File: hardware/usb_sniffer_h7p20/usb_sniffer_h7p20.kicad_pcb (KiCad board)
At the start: 4 copper layers, 45 x 45 mm, 149 parts, among them J2 USB_C_Receptacle_USB2.0_16P, J3 USB_A, J4 USB_C_Receptacle_USB2.0_16P, J5 FFC-40P-0.5mm,NC, U1 H7P20N0L128-M3H1, U11 EA3036C, U2 LM2903, U3 LM2903, U4 LM2903, U5 USB3343, U6 P25Q32SH-SSH-IT, U7 CY7C68013A-56LTX, U8 24C64BN, U9 CJ3439KDW, X1 XO32,26M,NC, Y1 26M,NC, Y2 24M

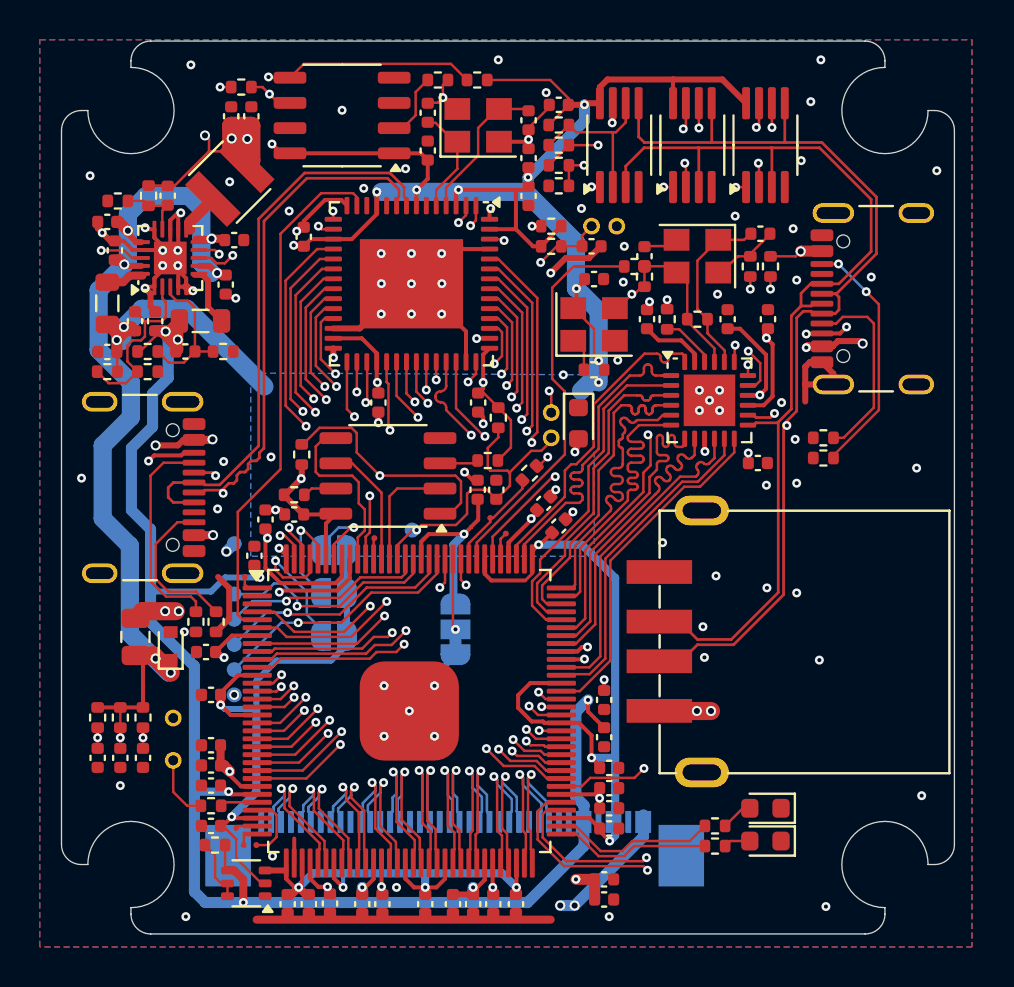
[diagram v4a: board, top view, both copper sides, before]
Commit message: [usb_sniffer_h7p20]增加JTAG排针，增加产品页二维码
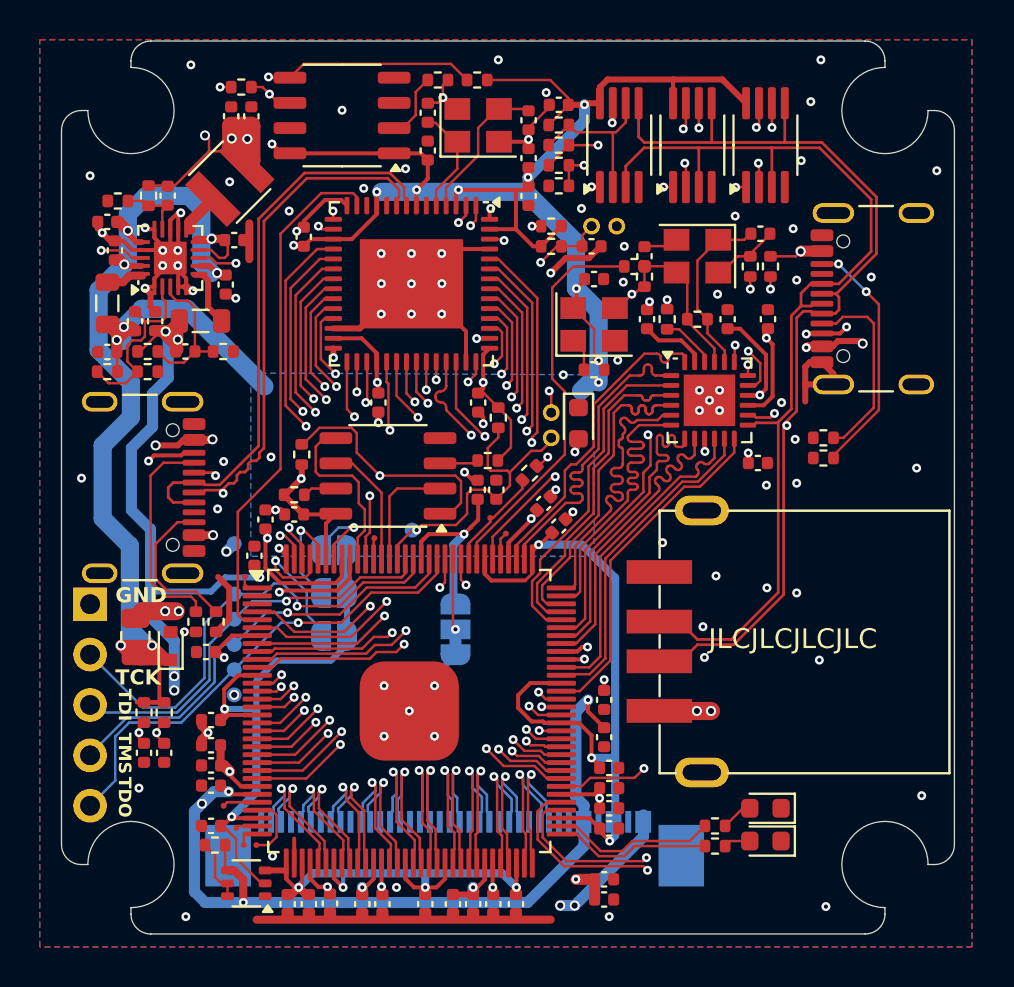
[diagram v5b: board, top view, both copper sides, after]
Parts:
- removed C40: NC, Capacitor_SMD:C_0402_1005Metric
- removed R36: NC, Resistor_SMD:R_0402_1005Metric
- removed R7: 470, Resistor_SMD:R_0402_1005Metric
- removed TP14, TP15: TestPoint, vllogic:PinHeader_1x01_P1.00mm_Vertical
- added G***: LOGO, LOGO, B.Cu at (107.6, 83.6)
- added J1: FPGA_JTAG, Connector_PinHeader_2.54mm:PinHeader_1x05_P2.54mm_Vertical, F.Cu at (91.4, 103.4)
- added TP5: TestPoint, vllogic:TestPoint_Pad_D0.3mm, F.Cu at (98.2, 113.5)
- moved C36 2.35 mm to (94.2, 110.9)
- moved R38 2.35 mm to (94.2, 108.8)
- moved C14 1.27 mm to (97.5, 109.2)
- moved C38 1.10 mm to (95.2, 110.9)
- moved R37 1.10 mm to (95.2, 108.8)
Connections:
- U1 pad 28: /B7_IO_28 -> Net-(U1-IO17_7)
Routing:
- net /VCC_5V: track 127.8 -> 101.0 mm, vias 11 -> 9
- net /FPGA_TCK: track 11.4 -> 23.7 mm
- net /FPGA_TDO: track 13.0 -> 24.4 mm
- net /FPGA_TMS: track 12.1 -> 22.6 mm
- net /FPGA_TDI: track 10.3 -> 20.8 mm
- net GND: track 82.8 -> 86.2 mm, vias 94 -> 95
- net Net-(R7-Pad1): track 3.27 -> 0.00 mm
- net /B7_IO_28: track 1.89 -> 0.00 mm
- net Net-(U1-IO17_7): track 0.00 -> 1.77 mm
- net /VCCAUX: track 97.7 -> 98.6 mm, vias 10 -> 13
- net /ET3036C/EA3036_EN2: track 34.0 -> 33.5 mm
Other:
- board text added: "GND"
- board text added: "JLCJLCJLCJLC"
- board text added: "TCK"
- board text added: "TDI"
- board text added: "TDO"
- board text added: "TMS"

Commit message: [usb_sniffer_h7p20] 结构优化与验证
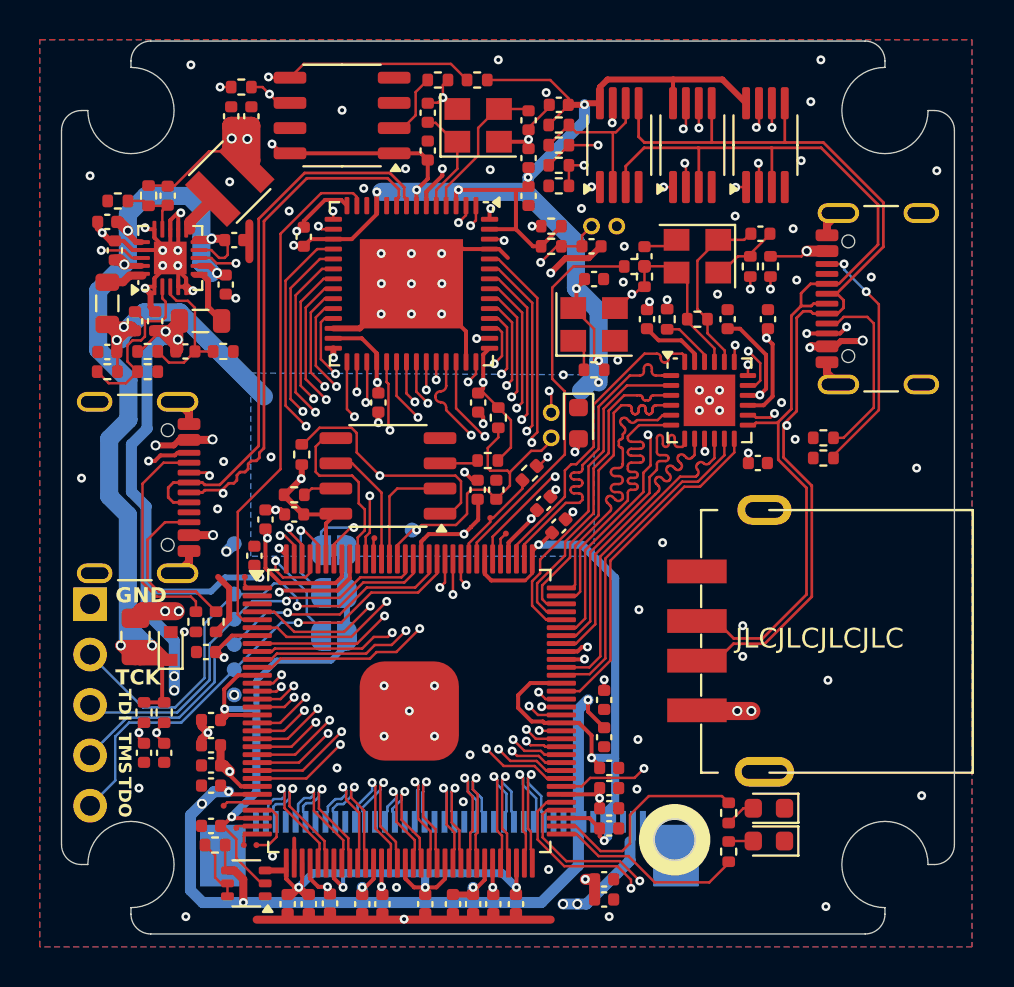
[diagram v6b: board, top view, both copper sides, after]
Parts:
- removed JP1: SolderJumper_3_Bridged12, Jumper:SolderJumper-3_P1.3mm_Bridged12_RoundedPad1.0x1.5mm_NumberLabels
- J3: footprint vllogic:USB-AF-180 -> vllogic:USB-AF_YIJIAN
- JP2: value SolderJumper_2_Open -> SolderJumper_2_Bridged; footprint Jumper:SolderJumper-2_P1.3mm_Open_RoundedPad1.0x1.5mm -> Jumper:SolderJumper-2_P1.3mm_Bridged_RoundedPad1.0x1.5mm
- moved J3 2.09 mm to (122.2, 105.2)
- moved R8 0.95 mm to (123.6, 113.9), turned to 90 degrees
- moved R9 0.74 mm to (123.6, 115.8), turned to -90 degrees
- moved J5 0.26 mm to (109.5, 115.7)
- moved J4 0.25 mm to (92.7, 97.5)
- moved J2 0.25 mm to (132.3, 88.0)
- moved D2 0.17 mm to (125.7, 113.7)
- moved D3 0.17 mm to (125.7, 115.3)
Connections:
- J5 pad 1: /VCC_5V -> unconnected-(J5-Pin_1-Pad1)
- U1 pad 107: /MSC -> GND
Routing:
- net /VCC_3V3: track 213.7 -> 209.7 mm
- net /MSC: track 3.60 -> 0.00 mm, vias 1 -> 0
- net /LED_RED: track 8.28 -> 11.1 mm
- net /USB20_DM_CMP2: track 62.8 -> 65.4 mm
- net /USB20_DM_CMP1: track 57.0 -> 59.5 mm
- net /VCCAUX: track 98.6 -> 101.0 mm
- net /USB20_DP_CMP1: track 49.0 -> 51.3 mm
- net /LED_BLUE: track 7.91 -> 9.91 mm
- net /B10_IO12P: track 7.78 -> 5.92 mm
- net /B10_IO12N: track 7.78 -> 5.92 mm
- net /B9_IO4N: track 7.70 -> 5.85 mm
- net /B9_IO4P: track 7.70 -> 5.86 mm
- net GND: track 86.2 -> 87.4 mm, vias 95 -> 101
- net /B9_IO2P: track 7.64 -> 6.60 mm
- net /B9_IO2N: track 7.64 -> 6.60 mm
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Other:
- outline, holes or cut-outs redrawn
- board text added: "USB Sniffer H7P20 20250615"
- board text removed: "USB Sniffer H7P20 20250606"

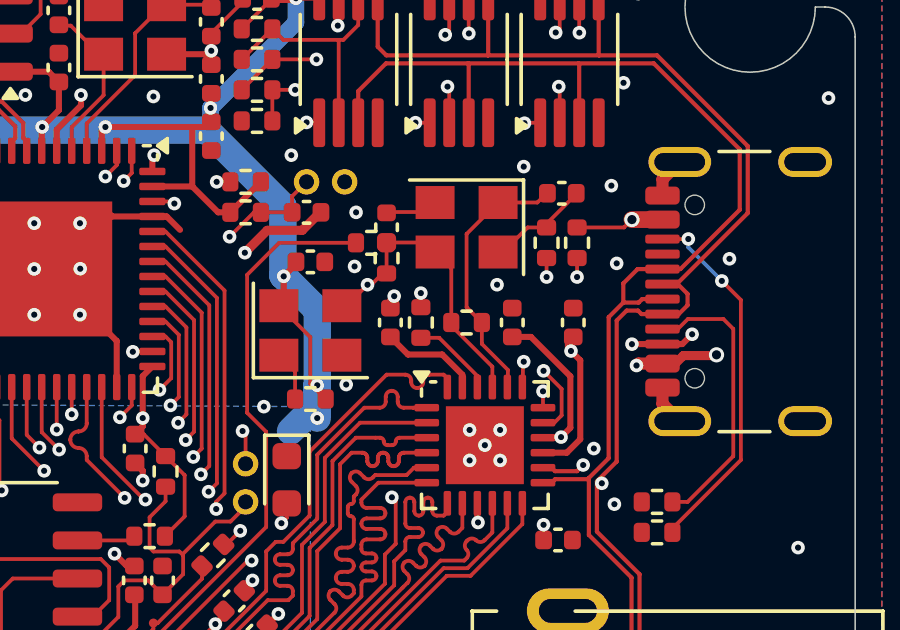
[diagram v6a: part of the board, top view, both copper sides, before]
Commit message: [usb_sniffer_h7p20] 修复USB3343参考时钟电路错误；修复USB3343 RESET脚上拉错误
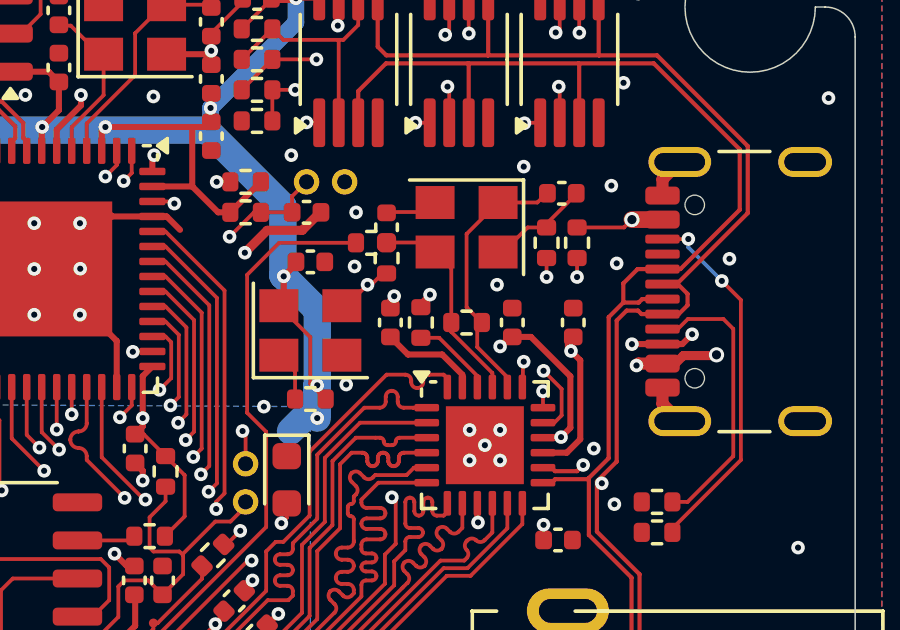
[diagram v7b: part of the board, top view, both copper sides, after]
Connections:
- C7 pad 2: /XO32_26M -> /USB334x_26M
- R14 pad 2: /XO32_26M -> /USB334x_26M
- R27 pad 2: /XO32_26M -> /USB334x_26M
- R29 pad 2: /XO32_26M -> /USB334x_26M
- R31 pad 1: Net-(U5-ID) -> /VCC_3V3
- U5 pad 21: /XO32_26M -> /USB334x_26M
- Y1 pad 3: /XO32_26M -> /USB334x_26M
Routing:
- net /XO32_26M: track 29.6 -> 21.6 mm
- net /USB334x_26M: track 0.00 -> 7.05 mm
- net Net-(U5-ID): track 13.3 -> 7.36 mm, vias 3 -> 2
- net /VCC_3V3: track 209.7 -> 213.8 mm, vias 26 -> 28
